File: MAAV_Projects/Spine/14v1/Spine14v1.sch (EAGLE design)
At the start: 91 parts, among them J7 MA04-1, Q1 MOSFET-NCHANNELSMD, Q2 MOSFET-NCHANNELSMD, Q21 P-MOSFET-SO8POWER-PAK, Q22 P-MOSFET-SO8POWER-PAK, Q23 P-MOSFET-SO8POWER-PAK, Q24 P-MOSFET-SO8POWER-PAK, Q3 MOSFET-NCHANNELSMD, Q4 MOSFET-NCHANNELSMD, Q5 P-MOSFET-SO8POWER-PAK, Q6 MOSFET-NCHANNELSMD, Q7 MOSFET-NCHANNELSMD, Q8 MOSFET-NCHANNELSMD, U1 ATMEGA328-AU, U3 XC6210

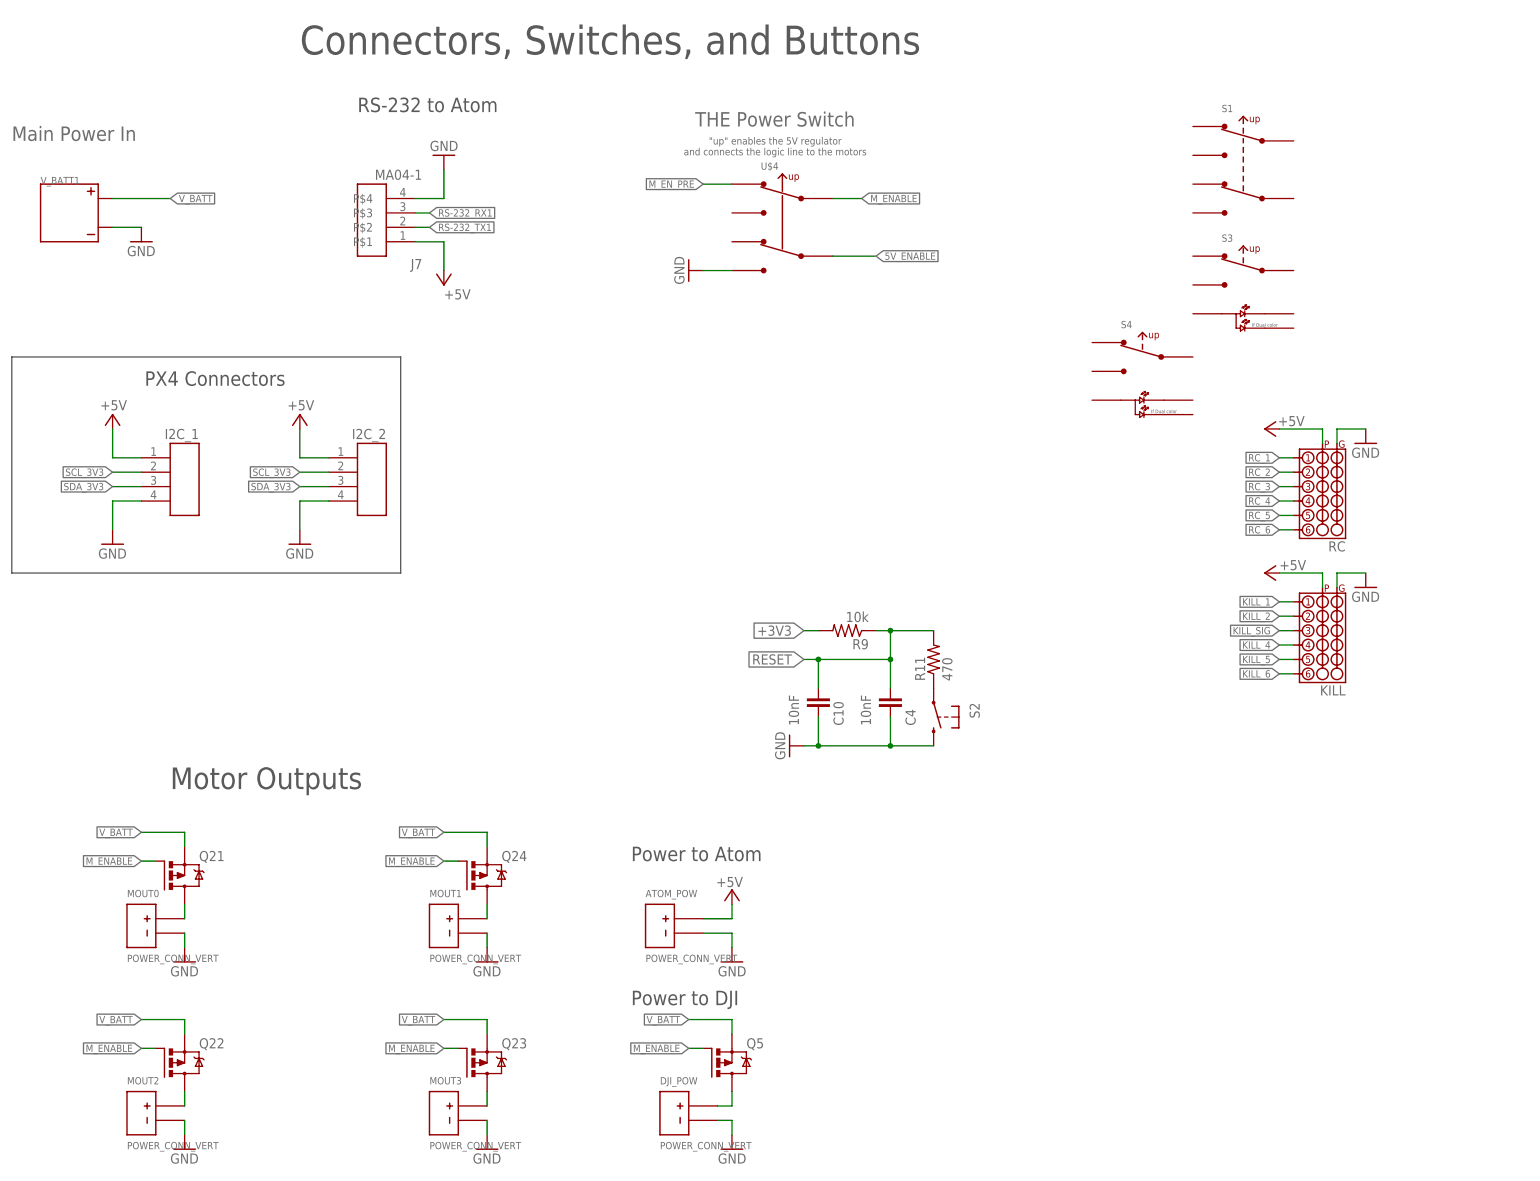
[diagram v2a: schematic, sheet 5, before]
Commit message: finished JTAG routing. still need to finish the toggle switches
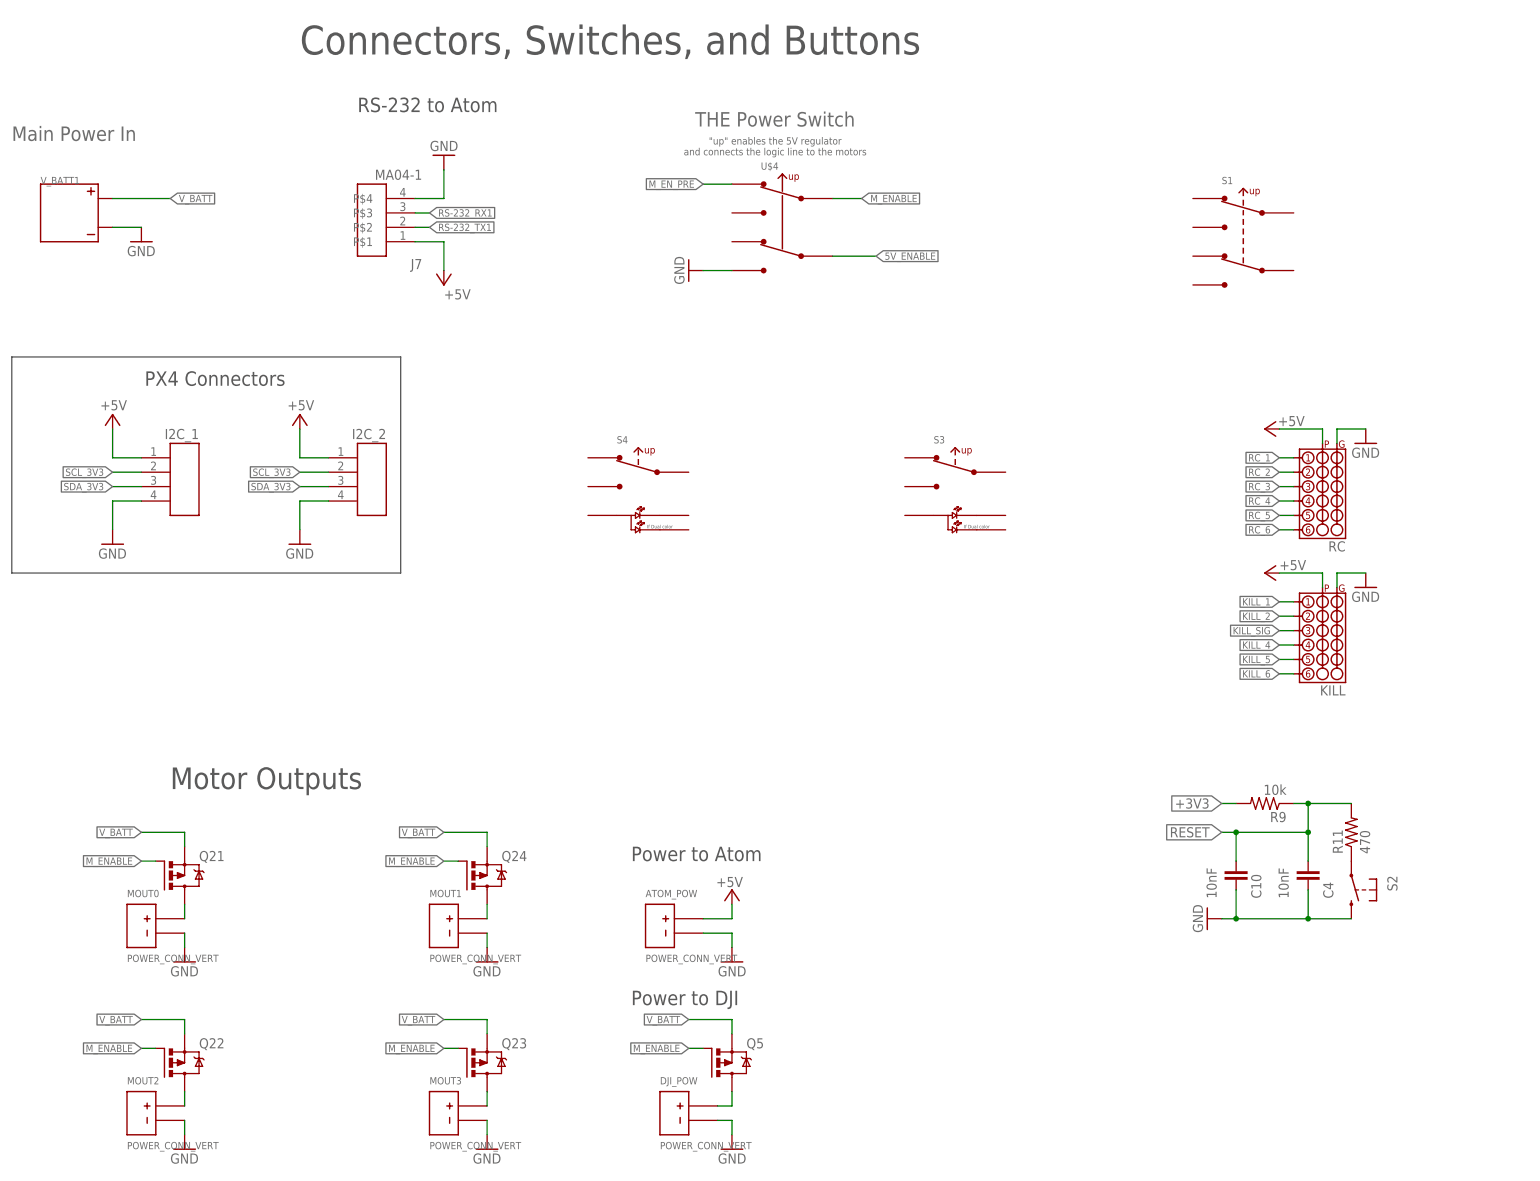
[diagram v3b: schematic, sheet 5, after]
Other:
- moved on the sheet: C10, C4, R11, R9, S1, S2, S3, S4
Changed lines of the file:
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@@
 <?xml version="1.0" encoding="utf-8"?>
 <!DOCTYPE eagle SYSTEM "eagle.dtd">
-<eagle version="6.4">
+<eagle version="6.5.0">
 <drawing>
 <settings>
@@
 <instance part="V_BATT1" gate="G$1" x="25.4" y="172.72"/>
 <instance part="GND4" gate="1" x="38.1" y="167.64"/>
-<instance part="R9" gate="G$1" x="162.56" y="99.06" rot="R180"/>
-<instance part="GND9" gate="1" x="152.4" y="78.74" rot="R270"/>
-<instance part="C4" gate="G$1" x="170.18" y="86.36" smashed="yes">
-<attribute name="NAME" x="174.625" y="82.296" size="1.778" layer="95" rot="R90"/>
-<attribute name="VALUE" x="166.751" y="82.296" size="1.778" layer="96" rot="R90"/>
-</instance>
-<instance part="R11" gate="G$1" x="177.8" y="93.98" rot="R90"/>
+<instance part="R9" gate="G$1" x="236.22" y="68.58" rot="R180"/>
+<instance part="GND9" gate="1" x="226.06" y="48.26" rot="R270"/>
+<instance part="C4" gate="G$1" x="243.84" y="55.88" smashed="yes">
+<attribute name="NAME" x="248.285" y="51.816" size="1.778" layer="95" rot="R90"/>
+<attribute name="VALUE" x="240.411" y="51.816" size="1.778" layer="96" rot="R90"/>
+</instance>
+<instance part="R11" gate="G$1" x="251.46" y="63.5" rot="R90"/>
 <instance part="GND43" gate="1" x="45.72" y="40.64"/>
 <instance part="MOUT0" gate="G$1" x="40.64" y="48.26"/>
@@
 <instance part="GND27" gate="1" x="142.24" y="7.62" rot="MR0"/>
 <instance part="Q5" gate="G$1" x="139.7" y="22.86"/>
-<instance part="C10" gate="G$1" x="157.48" y="86.36" smashed="yes">
-<attribute name="NAME" x="161.925" y="82.296" size="1.778" layer="95" rot="R90"/>
-<attribute name="VALUE" x="154.051" y="82.296" size="1.778" layer="96" rot="R90"/>
-</instance>
-<instance part="S2" gate="1" x="177.8" y="83.82" rot="R180"/>
+<instance part="C10" gate="G$1" x="231.14" y="55.88" smashed="yes">
+<attribute name="NAME" x="235.585" y="51.816" size="1.778" layer="95" rot="R90"/>
+<attribute name="VALUE" x="227.711" y="51.816" size="1.778" layer="96" rot="R90"/>
+</instance>
+<instance part="S2" gate="1" x="251.46" y="53.34" rot="R180"/>
 <instance part="ATOM_POW" gate="G$1" x="132.08" y="48.26"/>
 <instance part="GND36" gate="1" x="142.24" y="40.64" rot="MR0"/>
@@
 <attribute name="VALUE" x="139.446" y="53.848" size="1.778" layer="96"/>
 </instance>
-<instance part="S1" gate="G$1" x="231.14" y="180.34"/>
-<instance part="S3" gate="G$1" x="231.14" y="157.48"/>
-<instance part="S4" gate="G$1" x="213.36" y="142.24"/>
+<instance part="S1" gate="G$1" x="231.14" y="167.64"/>
+<instance part="S3" gate="G$1" x="180.34" y="121.92"/>
+<instance part="S4" gate="G$1" x="124.46" y="121.92"/>
 </instances>
 <busses>
@@
 <segment>
 <pinref part="GND9" gate="1" pin="GND"/>
-<wire x1="154.94" y1="78.74" x2="157.48" y2="78.74" width="0.1524" layer="91"/>
+<wire x1="228.6" y1="48.26" x2="231.14" y2="48.26" width="0.1524" layer="91"/>
 <pinref part="S2" gate="1" pin="S"/>
-<wire x1="157.48" y1="78.74" x2="170.18" y2="78.74" width="0.1524" layer="91"/>
-<wire x1="170.18" y1="78.74" x2="177.8" y2="78.74" width="0.1524" layer="91"/>
+<wire x1="231.14" y1="48.26" x2="243.84" y2="48.26" width="0.1524" layer="91"/>
+<wire x1="243.84" y1="48.26" x2="251.46" y2="48.26" width="0.1524" layer="91"/>
 <pinref part="C4" gate="G$1" pin="2"/>
-<wire x1="170.18" y1="83.82" x2="170.18" y2="78.74" width="0.1524" layer="91"/>
-<junction x="170.18" y="78.74"/>
+<wire x1="243.84" y1="53.34" x2="243.84" y2="48.26" width="0.1524" layer="91"/>
+<junction x="243.84" y="48.26"/>
 <pinref part="C10" gate="G$1" pin="2"/>
-<wire x1="157.48" y1="83.82" x2="157.48" y2="78.74" width="0.1524" layer="91"/>
-<junction x="157.48" y="78.74"/>
+<wire x1="231.14" y1="53.34" x2="231.14" y2="48.26" width="0.1524" layer="91"/>
+<junction x="231.14" y="48.26"/>
 </segment>
 <segment>
@@
 <pinref part="C4" gate="G$1" pin="1"/>
 <pinref part="R9" gate="G$1" pin="1"/>
-<wire x1="170.18" y1="88.9" x2="170.18" y2="93.98" width="0.1524" layer="91"/>
+<wire x1="243.84" y1="58.42" x2="243.84" y2="63.5" width="0.1524" layer="91"/>
 <pinref part="R11" gate="G$1" pin="2"/>
-<junction x="170.18" y="93.98"/>
-<wire x1="170.18" y1="93.98" x2="157.48" y2="93.98" width="0.1524" layer="91"/>
-<label x="154.94" y="93.98" size="1.778" layer="95" rot="R180" xref="yes"/>
+<junction x="243.84" y="63.5"/>
+<wire x1="243.84" y1="63.5" x2="231.14" y2="63.5" width="0.1524" layer="91"/>
+<label x="228.6" y="63.5" size="1.778" layer="95" rot="R180" xref="yes"/>
 <pinref part="C10" gate="G$1" pin="1"/>
-<wire x1="157.48" y1="93.98" x2="154.94" y2="93.98" width="0.1524" layer="91"/>
-<wire x1="157.48" y1="88.9" x2="157.48" y2="93.98" width="0.1524" layer="91"/>
-<junction x="157.48" y="93.98"/>
-<wire x1="167.64" y1="99.06" x2="170.18" y2="99.06" width="0.1524" layer="91"/>
-<wire x1="170.18" y1="99.06" x2="177.8" y2="99.06" width="0.1524" layer="91"/>
-<wire x1="170.18" y1="99.06" x2="170.18" y2="93.98" width="0.1524" layer="91"/>
-<junction x="170.18" y="99.06"/>
+<wire x1="231.14" y1="63.5" x2="228.6" y2="63.5" width="0.1524" layer="91"/>
+<wire x1="231.14" y1="58.42" x2="231.14" y2="63.5" width="0.1524" layer="91"/>
+<junction x="231.14" y="63.5"/>
+<wire x1="241.3" y1="68.58" x2="243.84" y2="68.58" width="0.1524" layer="91"/>
+<wire x1="243.84" y1="68.58" x2="251.46" y2="68.58" width="0.1524" layer="91"/>
+<wire x1="243.84" y1="68.58" x2="243.84" y2="63.5" width="0.1524" layer="91"/>
+<junction x="243.84" y="68.58"/>
 </segment>
 </net>
@@
 <segment>
 <pinref part="R9" gate="G$1" pin="2"/>
-<wire x1="157.48" y1="99.06" x2="154.94" y2="99.06" width="0.1524" layer="91"/>
-<label x="154.94" y="99.06" size="1.778" layer="95" rot="R180" xref="yes"/>
-</segment>
-</net>
+<wire x1="231.14" y1="68.58" x2="228.6" y2="68.58" width="0.1524" layer="91"/>
+<label x="228.6" y="68.58" size="1.778" layer="95" rot="R180" xref="yes"/>
+</segment>
+</net>

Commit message: put in toggle switches and finished routing the baord.  Added logo and credits
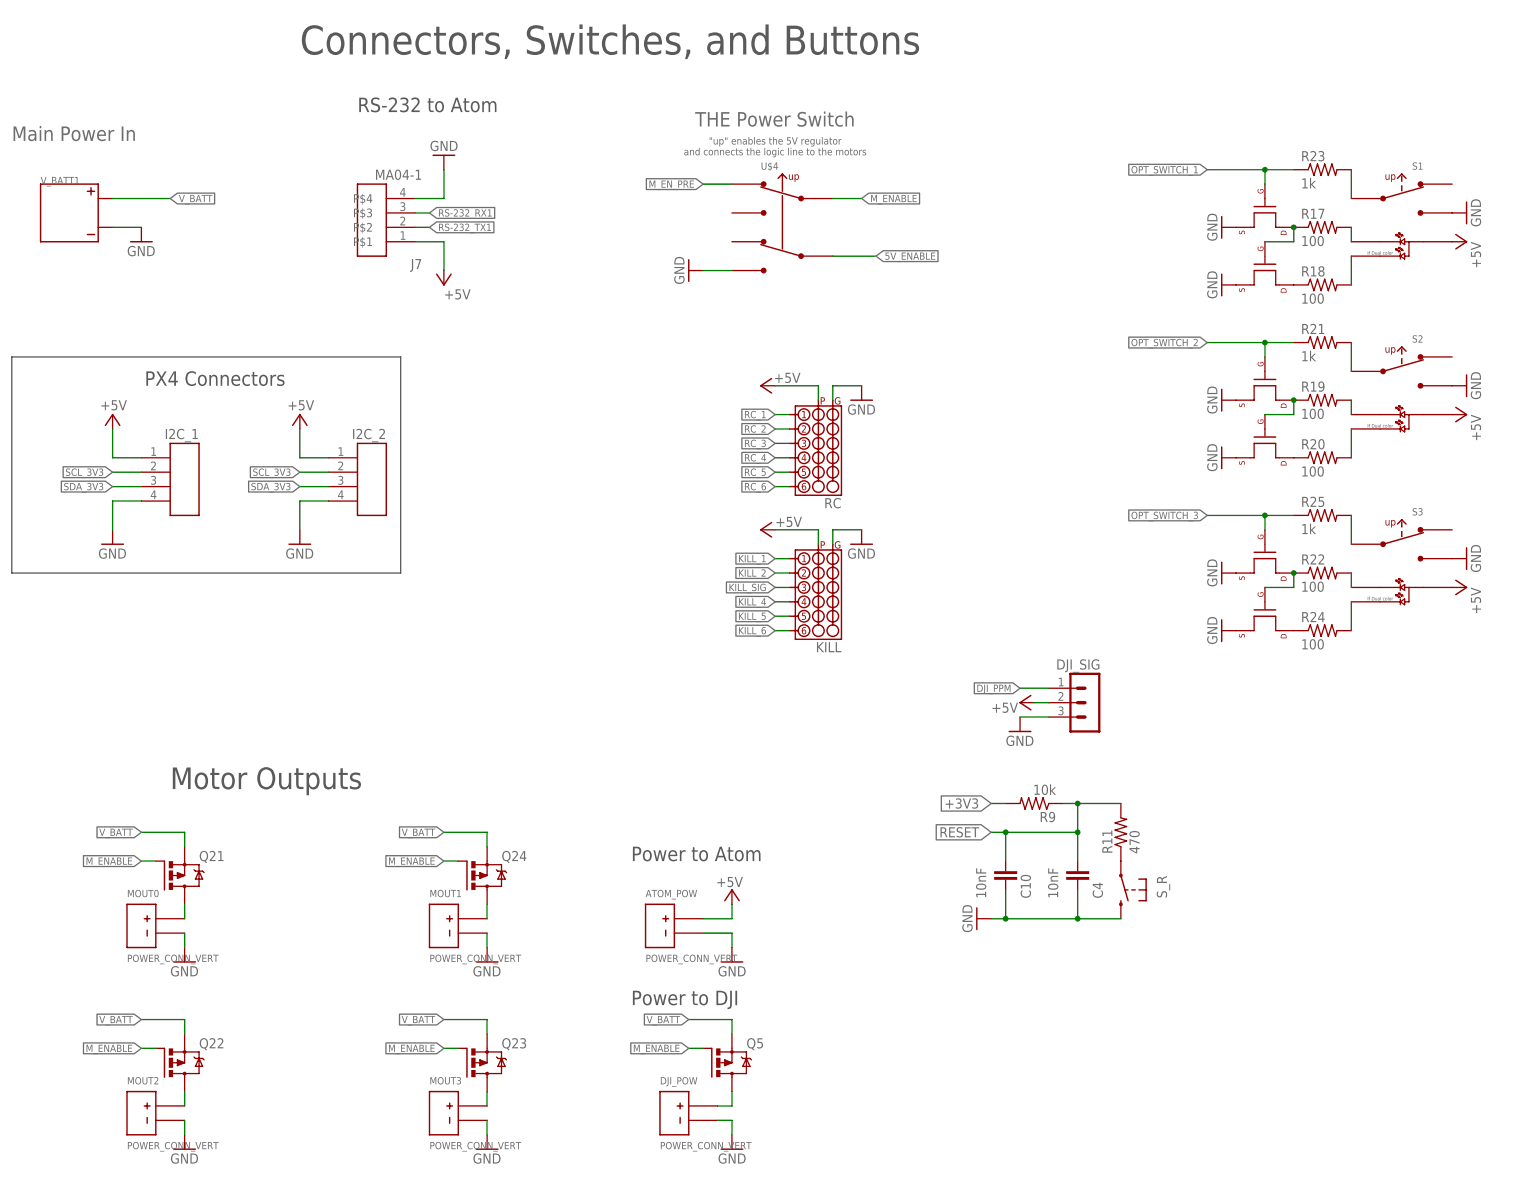
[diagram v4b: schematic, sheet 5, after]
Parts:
- removed S4: SWITCH_SPDT_ILUMINATED_2COLOR_VERT_ILLUMINATED, Jon_LIB:SWITCH_SPDT_ILUMINATED_2COLOR_VERT_ILLUMINATED
- added DJI_SIG: (no value), Jon_LIB:MA03-1
- added Q10, Q11, Q12, Q13, Q14, Q9: MOSFET-NCHANNELSMD, Jon_LIB:MOSFET-NCHANNELSMD
- added R17, R18, R19, R20, R22, R24: 100, Jon_LIB:R-USR0603
- added R21, R23, R25: 1k, Jon_LIB:R-USR0603
- added S_R: (no value), Jon_LIB:TACT_BUTTONSMD
- S1: value SWITCH_DPDT_VERT_TOGGLE -> SWITCH_SPDT_ILUMINATED_2COLOR_VERT_ILLUMINATED; device Jon_LIB:SWITCH_DPDT_VERT_TOGGLE -> Jon_LIB:SWITCH_SPDT_ILUMINATED_2COLOR_VERT_ILLUMINATED
- S2: value (none) -> SWITCH_SPDT_ILUMINATED_2COLOR_VERT_ILLUMINATED; device Jon_LIB:TACT_BUTTONSMD -> Jon_LIB:SWITCH_SPDT_ILUMINATED_2COLOR_VERT_ILLUMINATED
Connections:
- new net DJI_PPM: DJI_SIG.1, U$3.PB6
- new net N$26: Q9.D, R18.1
- new net N$27: Q11.G, Q12.D, R19.1
- new net N$28: Q11.D, R20.1
- new net N$29: R19.2, S2.P$6
- new net N$30: R20.2, S2.P$4
- new net N$31: R23.2, S1.P$2
- new net N$33: R21.2, S2.P$2
- new net N$34: R17.2, S1.P$6
- new net N$37: R18.2, S1.P$4
- new net N$39: Q13.G, Q14.D, R22.1
- new net N$40: Q13.D, R24.1
- new net N$41: R22.2, S3.P$6
- new net N$42: R24.2, S3.P$4
- new net N$43: R25.2, S3.P$2
- new net N$9: Q10.D, Q9.G, R17.1
- new net OPT_SWITCH_1: Q10.G, R23.1, U$3.PB1/USB0VBUS
- new net OPT_SWITCH_2: Q12.G, R21.1, U$3.PB2/I2C0SCL
- new net OPT_SWITCH_3: Q14.G, R25.1, U$3.PB3/I2C0SDA
- net +5V: now also DJI_SIG.2, S1.P$5, S2.P$5, S3.P$5
- net GND: now also DJI_SIG.3, Q10.S, Q11.S, Q12.S, Q13.S, Q14.S, Q9.S, S1.P$1, S2.P$1, S3.P$1, S_R.S; no longer S2.S
- net N$10: now also S_R.P; no longer S2.P
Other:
- note removed: "Check the sizes used in last years design"
- note removed: "Still need... signal to DJI"
- note removed: "Switch to Molex Sabre series WM9558-ND WM18463-ND WM18468-ND WM9174CT-ND WM9171CT-ND"
- moved on the sheet: C10, C4, KILL, R11, R9, RC, S3
